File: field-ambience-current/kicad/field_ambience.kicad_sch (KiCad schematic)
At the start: 0 parts

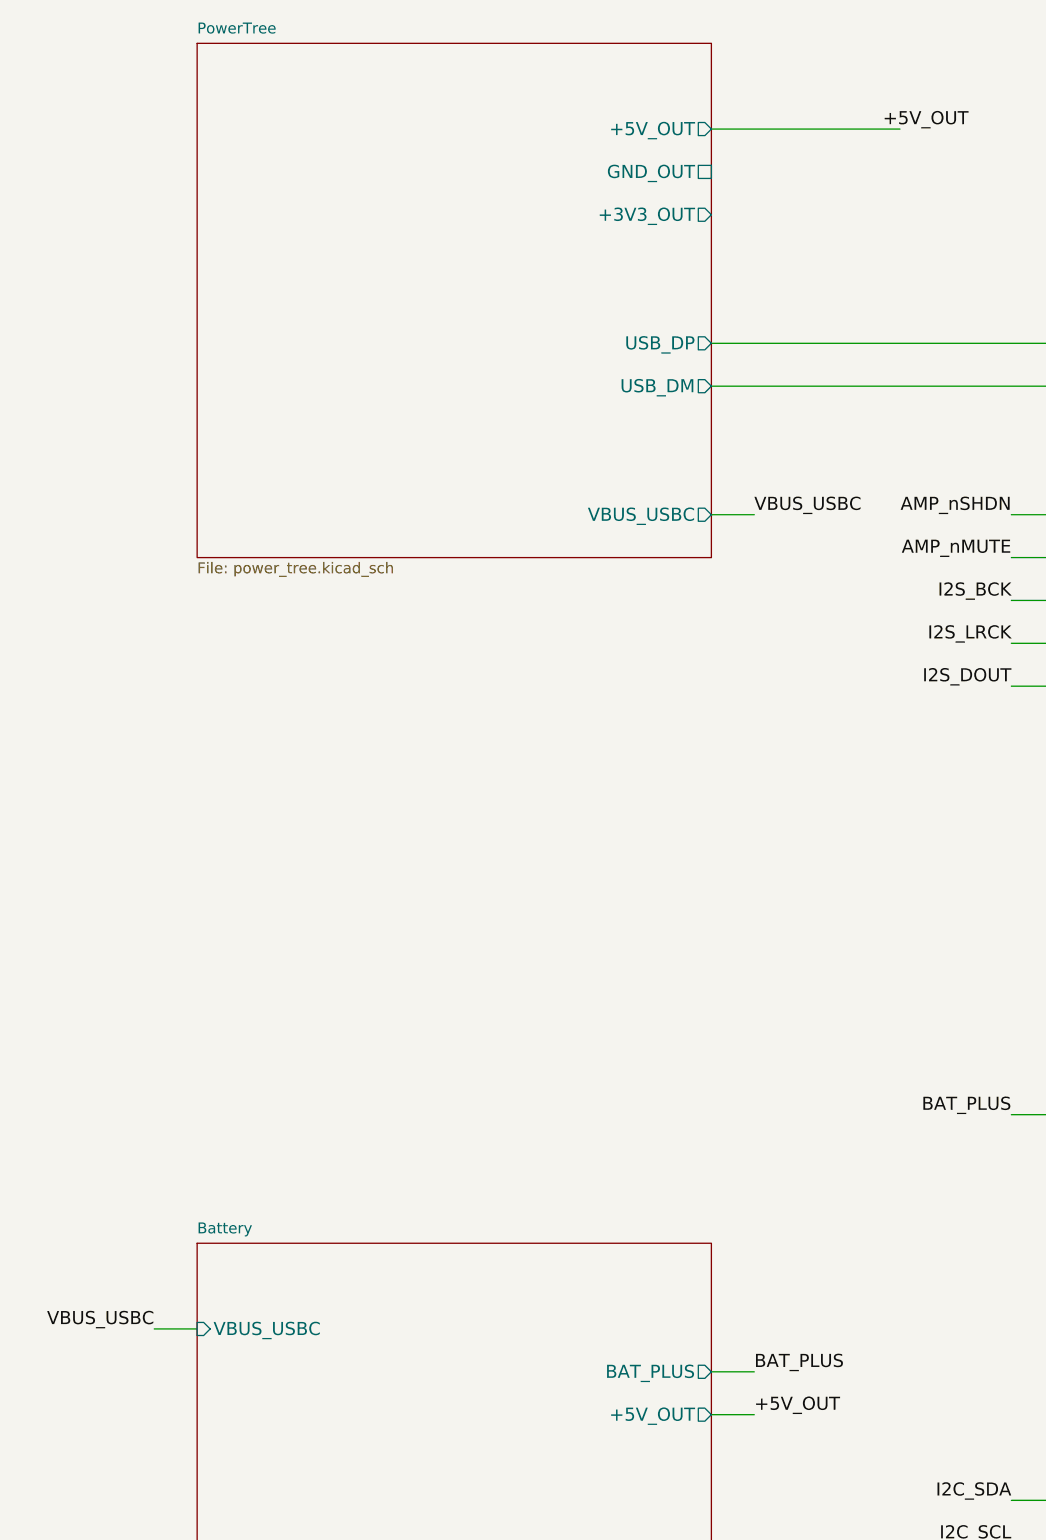
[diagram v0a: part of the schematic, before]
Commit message: feat(hw): BQ24074 power-path replaces MCP73831 + diode-OR — all audit P0 fixed (r19.18, ADR-0023)
External hardware audit verdict was DO NOT FABRICATE; every checkable P0
was confirmed against the extracted netlist, then fixed at the generator:

- U7 = BQ24074RGTR (C54313, live-verified stock + JLC assembly):
  USB->F1->VBUS_FUSED->IN; OUT=VSYS->TPS61089->D3->+5V rail (single
  source, D3B diode-OR deleted); BAT<-F2 PTC (SMD1812P260TF/16,
  C438899)<-J9. Values per TI SLUS810N: ICHG 0.89A (R_ISET 1k),
  IIN 1.34A (R_ILIM_IN 1.2k YAGEO C114605), ITERM/TMR=NC defaults,
  TS=10k fixed, EN2=VSYS/EN1=GND, CE_N=GND, EP->VSS.
- Boost EN = PWR_ON (was always-on battery drain); SW_PWR pull source
  moved to VSYS (rail-sourced pull would deadlock); LED_CHRG now fed
  from VBUS_FUSED via CHG open-drain; rail bulk sits behind the boost
  (USB hot-plug sees only 4.7uF).
- New inter-sheet nets VBUS_FUSED/VSYS/PWR_ON via root; +5V_OUT is now
  an input on the power tree. TP_VSYS test point added.
- Footprint QFN-16-1EP_3x3mm_P0.5mm_EP1.7x1.7mm matched against the
  JLC/EasyEDA land pattern for C54313 (pitch/pads/EP identical).
- J4 SWD = DNP debug pads (bogus TC2030-IDC MPN + LCSC "TBD" removed
  from the order BOM); J8 explicitly LINE OUT; mechanical doc battery
  corrected 5000->2000 mAh.
- Validation: geometric netlist extractor over all 7 sheets — 157 nets,
  620 pins, 0 floating; check_pinmap green; host suite green (32 suites).
- Docs: ADR-0023, CHANGELOG r19.18, PROJECT_STATUS banner, SCHEMATIC_
  WALKTHROUGH §1/§7 rewritten, PINMAP/BRING_UP/BOM_MASTER/PCB_BOM/
  COST/SOURCING/OBJECTIVES/COMPONENT_LINKS/FOOTPRINT_RISK updated.

Co-Authored-By: Claude Fable 5 <noreply@anthropic.com>
Claude-Session: https://claude.ai/code/session_019pKguH6aG4iazMCWJnpmMn
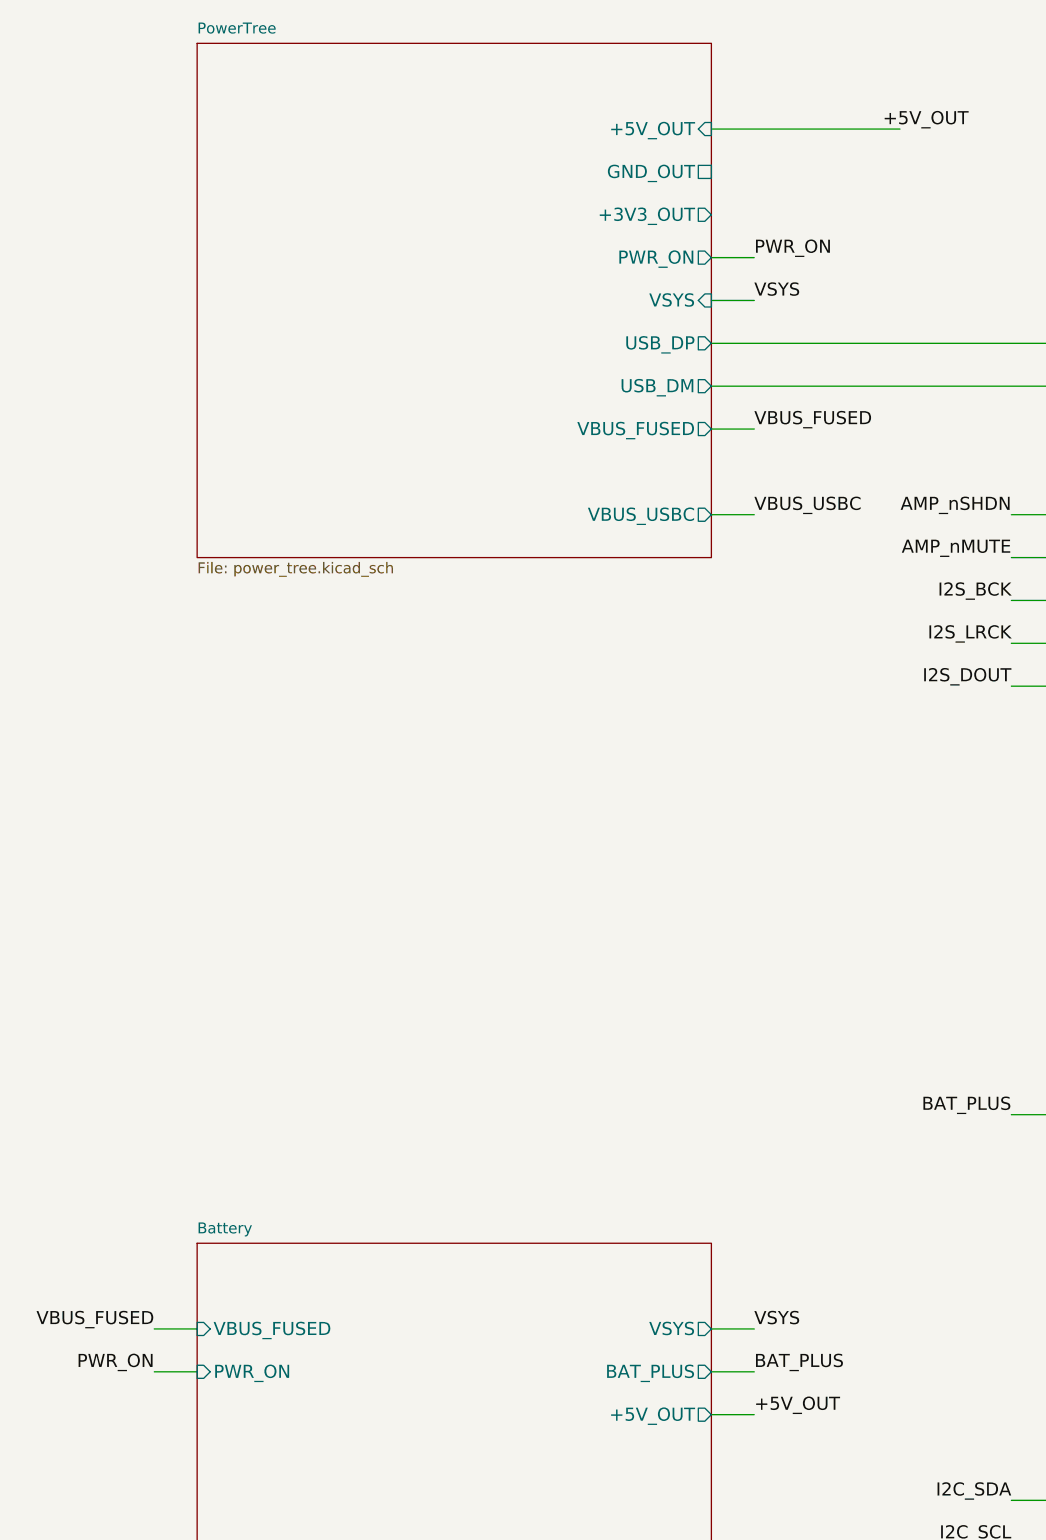
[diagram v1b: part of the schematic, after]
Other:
- sheet Battery ports: added PWR_ON, VBUS_FUSED, VSYS; removed VBUS_USBC
- sheet PowerTree ports: added PWR_ON, VBUS_FUSED, VSYS; removed none
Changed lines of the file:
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@@
     (property "Sheetfile" "power_tree.kicad_sch" (at 30 100.5 0)
       (effects (font (size 1.27 1.27)) (justify left top)))
-    (pin "+5V_OUT" output (at 90 50 0)
+    (pin "+5V_OUT" input (at 90 50 0)
       (effects (font (size 1.524 1.524)) (justify right))
 )
@@
       (effects (font (size 1.524 1.524)) (justify right))
 )
+    (pin "PWR_ON" output (at 90 65 0)
+      (effects (font (size 1.524 1.524)) (justify right))
+)
+    (pin "VSYS" input (at 90 70 0)
+      (effects (font (size 1.524 1.524)) (justify right))
+)
     (pin "USB_DP" output (at 90 75 0)
       (effects (font (size 1.524 1.524)) (justify right))
 )
     (pin "USB_DM" output (at 90 80 0)
+      (effects (font (size 1.524 1.524)) (justify right))
+)
+    (pin "VBUS_FUSED" output (at 90 85 0)
       (effects (font (size 1.524 1.524)) (justify right))
 )
@@
     (property "Sheetfile" "battery.kicad_sch" (at 30 220.5 0)
       (effects (font (size 1.27 1.27)) (justify left top)))
-    (pin "VBUS_USBC" input (at 30 190 180)
+    (pin "VBUS_FUSED" input (at 30 190 180)
+      (effects (font (size 1.524 1.524)) (justify left))
+)
+    (pin "PWR_ON" input (at 30 195 180)
       (effects (font (size 1.524 1.524)) (justify left))
 )
     (pin "BAT_PLUS" output (at 90 195 0)
+      (effects (font (size 1.524 1.524)) (justify right))
+)
+    (pin "VSYS" output (at 90 190 0)
       (effects (font (size 1.524 1.524)) (justify right))
 )
@@
   (wire (pts (xy 90 95) (xy 95 95)) (stroke (width 0) (type default)))
   (label "VBUS_USBC" (at 95 95 0) (effects (font (size 1.524 1.524)) (justify left bottom)))
-  (wire (pts (xy 25 190) (xy 30 190)) (stroke (width 0) (type default)))
-  (label "VBUS_USBC" (at 25 190 0) (effects (font (size 1.524 1.524)) (justify right bottom)))
   (wire (pts (xy 125 225) (xy 130 225)) (stroke (width 0) (type default)))
   (label "VBUS_USBC" (at 125 225 0) (effects (font (size 1.524 1.524)) (justify right bottom)))
+  (wire (pts (xy 90 85) (xy 95 85)) (stroke (width 0) (type default)))
+  (label "VBUS_FUSED" (at 95 85 0) (effects (font (size 1.524 1.524)) (justify left bottom)))
+  (wire (pts (xy 25 190) (xy 30 190)) (stroke (width 0) (type default)))
+  (label "VBUS_FUSED" (at 25 190 0) (effects (font (size 1.524 1.524)) (justify right bottom)))
+  (wire (pts (xy 90 65) (xy 95 65)) (stroke (width 0) (type default)))
+  (label "PWR_ON" (at 95 65 0) (effects (font (size 1.524 1.524)) (justify left bottom)))
+  (wire (pts (xy 25 195) (xy 30 195)) (stroke (width 0) (type default)))
+  (label "PWR_ON" (at 25 195 0) (effects (font (size 1.524 1.524)) (justify right bottom)))
+  (wire (pts (xy 90 190) (xy 95 190)) (stroke (width 0) (type default)))
+  (label "VSYS" (at 95 190 0) (effects (font (size 1.524 1.524)) (justify left bottom)))
+  (wire (pts (xy 90 70) (xy 95 70)) (stroke (width 0) (type default)))
+  (label "VSYS" (at 95 70 0) (effects (font (size 1.524 1.524)) (justify left bottom)))
   (wire (pts (xy 90 195) (xy 95 195)) (stroke (width 0) (type default)))
   (label "BAT_PLUS" (at 95 195 0) (effects (font (size 1.524 1.524)) (justify left bottom)))
